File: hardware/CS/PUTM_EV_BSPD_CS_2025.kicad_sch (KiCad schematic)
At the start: 30 parts, among them J1 Conn_01x04, J2 LEM, J3 Conn_01x04, U1 MC78M12CDTG, U2 LM1117IMP-5.0, U3 TLV9354QPWRQ1

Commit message: initial layout for Current Sensor
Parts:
- removed J1: Conn_01x04, symbol Connector_Generic:Conn_01x04
- 24V/500mA1: renamed from 24V/500mA; footprint (none) -> Fuse:Fuse_1812_4532Metric
- C1: footprint (none) -> Capacitor_SMD:C_0805_2012Metric
- C7: footprint (none) -> Capacitor_SMD:C_0603_1608Metric
- D1: footprint Diode_THT:D_DO-201AE_P15.24mm_Horizontal -> Diode_SMD:D_SOD-523
- D2, D3: footprint (none) -> Diode_SMD:D_0603_1608Metric
- J2: footprint (none) -> Snapeda:current_sensor
- J3: footprint (none) -> Snapeda:HARWIN_M80-5100422
- R1, R10, R11, R12, R13, R2, R3, R4, R5, R6, R7, R8, R9: footprint (none) -> Resistor_SMD:R_0603_1608Metric
- U3: footprint (none) -> Snapeda:DYY0014A_TEX-M
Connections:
- net OUT: now reaches U3.13 (-), U3.14
- net OUT: now also J3.3 (Pin_3)
- no-connect marks 4 -> 1
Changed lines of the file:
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@@
 	)
 	(no_connect
-		(at 26.67 27.94)
-	)
-	(no_connect
-		(at 228.6 111.76)
-	)
-	(no_connect
-		(at 228.6 114.3)
-	)
-	(no_connect
 		(at 26.67 30.48)
 	)
@@
 	(wire
 		(pts
+			(xy 26.67 27.94) (xy 29.21 27.94)
+		)
+		(stroke
+			(width 0)
+			(type default)
+		)
+	)
+	(wire
+		(pts
 			(xy 132.08 113.03) (xy 132.08 115.57)
 		)
@@
 		)
 	)
-	(symbol
-		(lib_id "Connector_Generic:Conn_01x04")
-		(at 233.68 111.76 0)
-		(unit 1)
-		(exclude_from_sim no)
-		(in_bom yes)
-		(on_board yes)
-		(dnp no)
-		(fields_autoplaced yes)
-		(property "Reference" "J1"
-			(at 236.22 111.7599 0)
-			(effects
-				(font
-					(size 1.27 1.27)
-				)
-				(justify left)
-			)
-		)
-		(property "Value" "Conn_01x04"
-			(at 236.22 114.2999 0)
-			(effects
-				(font
-					(size 1.27 1.27)
-				)
-				(justify left)
-			)
-		)
-		(property "Footprint" ""
-			(at 233.68 111.76 0)
-			(effects
-				(font
-					(size 1.27 1.27)
-				)
-				(hide yes)
-			)
-		)
-		(property "Datasheet" "~https://www.harwin.com/products/M80-4810405"
-			(at 233.68 111.76 0)
-			(effects
-				(font
-					(size 1.27 1.27)
-				)
-				(hide yes)
-			)
-		)
-		(property "Description" "Generic connector, single row, 01x04, script generated (kicad-library-utils/schlib/autogen/connector/)"
-			(at 233.68 111.76 0)
-			(effects
-				(font
-					(size 1.27 1.27)
-				)
-				(hide yes)
+	(label "OUT"
+		(at 228.6 109.22 0)
+		(effects
+			(font
+				(size 1.27 1.27)
 			)
+			(justify left bottom)
 		)
-		(pin "1"
-		)
-		(pin "3"
-		)
-		(pin "4"
-		)
-		(pin "2"
-		)
-		(instances
-			(project ""
-				(path "/b652b05a-4e3d-4ad1-b032-18886abe7d45"
-					(reference "J1")
-					(unit 1)
-				)
+	)
+	(label "OUT"
+		(at 29.21 27.94 0)
+		(effects
+			(font
+				(size 1.27 1.27)
 			)
+			(justify left bottom)
 		)
 	)
@@
 		(on_board yes)
 		(dnp no)
-		(property "Reference" "24V/500mA"
+		(property "Reference" "24V/500mA1"
 			(at 43.18 27.432 90)
 			(effects
@@
 			)
 		)
-		(property "Footprint" ""
+		(property "Footprint" "Fuse:Fuse_1812_4532Metric"
 			(at 43.18 27.178 90)
 			(effects
@@
 			(project "PUTM_EV_BSPD_CS_2025"
 				(path "/b652b05a-4e3d-4ad1-b032-18886abe7d45"
-					(reference "24V/500mA")
+					(reference "24V/500mA1")
 					(unit 1)
 				)
@@
 			)
 		)
-		(property "Footprint" ""
+		(property "Footprint" "Resistor_SMD:R_0603_1608Metric"
 			(at 178.308 92.71 90)
 			(effects
@@
 	)
 	(symbol
-		(lib_id "power:GND")
-		(at 228.6 116.84 270)
-		(unit 1)
-		(exclude_from_sim no)
-		(in_bom yes)
-		(on_board yes)
-		(dnp no)
-		(fields_autoplaced yes)
-		(property "Reference" "#PWR014"
-			(at 222.25 116.84 0)
-			(effects
-				(font
-					(size 1.27 1.27)
-				)
-				(hide yes)
-			)
-		)
-		(property "Value" "GND"
-			(at 224.79 116.8399 90)
-			(effects
-				(font
-					(size 1.27 1.27)
-				)
-				(justify right)
-			)
-		)
-		(property "Footprint" ""
-			(at 228.6 116.84 0)
-			(effects
-				(font
-					(size 1.27 1.27)
-				)
-				(hide yes)
-			)
-		)
-		(property "Datasheet" ""
-			(at 228.6 116.84 0)
-			(effects
-				(font
-					(size 1.27 1.27)
-				)
-				(hide yes)
-			)
-		)
-		(property "Description" "Power symbol creates a global label with name \"GND\" , ground"
-			(at 228.6 116.84 0)
-			(effects
-				(font
-					(size 1.27 1.27)
-				)
-				(hide yes)
-			)
-		)
-		(pin "1"
-		)
-		(instances
-			(project "PUTM_EV_BSPD_CS_2025"
-				(path "/b652b05a-4e3d-4ad1-b032-18886abe7d45"
-					(reference "#PWR014")
-					(unit 1)
-				)
-			)
-		)
-	)
-	(symbol
 		(lib_id "power:+5V")
 		(at 127 19.05 0)
@@
 			)
 		)
-		(property "Footprint" ""
+		(property "Footprint" "Snapeda:DYY0014A_TEX-M"
 			(at 105.41 106.68 0)
 			(effects
@@
 			)
 		)
-		(property "Footprint" ""
+		(property "Footprint" "Resistor_SMD:R_0603_1608Metric"
 			(at 252.222 24.13 90)
 			(effects
@@
 			)
 		)
-		(property "Footprint" ""
+		(property "Footprint" "Snapeda:DYY0014A_TEX-M"
 			(at 177.8 30.48 0)
 			(effects
@@
 			)
 		)
-		(property "Footprint" ""
+		(property "Footprint" "Resistor_SMD:R_0603_1608Metric"
 			(at 130.302 90.17 90)
 			(effects
@@
 			)
 		)
-		(property "Footprint" ""
+		(property "Footprint" "Resistor_SMD:R_0603_1608Metric"
 			(at 130.302 80.01 90)
 			(effects
@@
 			)
 		)
-		(property "Footprint" ""
+		(property "Footprint" "Resistor_SMD:R_0603_1608Metric"
 			(at 97.028 119.38 90)
 			(effects
@@
 			)
 		)
-		(property "Footprint" ""
+		(property "Footprint" "Diode_SMD:D_0603_1608Metric"
 			(at 176.53 111.76 0)
 			(effects
@@
 			)
 		)
-		(property "Footprint" ""
+		(property "Footprint" "Snapeda:DYY0014A_TEX-M"
 			(at 163.83 87.63 0)
 			(effects
@@
 			)
 		)
-		(property "Footprint" ""
+		(property "Footprint" "Snapeda:current_sensor"
 			(at 229.87 27.94 0)
 			(effects
@@
 			)
 		)
-		(property "Footprint" ""
+		(property "Footprint" "Resistor_SMD:R_0603_1608Metric"
 			(at 252.222 34.29 90)
 			(effects
@@
 			)
 		)
-		(property "Footprint" ""
+		(property "Footprint" "Resistor_SMD:R_0603_1608Metric"
 			(at 86.36 105.918 90)
 			(effects
@@
 			)
 		)
-		(property "Footprint" ""
+		(property "Footprint" "Diode_SMD:D_0603_1608Metric"
 			(at 176.53 100.33 0)
 			(effects
@@
 			)
 		)
-		(property "Footprint" ""
+		(property "Footprint" "Resistor_SMD:R_0603_1608Metric"
 			(at 139.7 108.458 90)
 			(effects
@@
 			)
 		)
-		(property "Footprint" ""
+		(property "Footprint" "Resistor_SMD:R_0603_1608Metric"
 			(at 86.36 110.998 90)
 			(effects
@@
 			)
 		)
-		(property "Footprint" ""
+		(property "Footprint" "Resistor_SMD:R_0603_1608Metric"
 			(at 178.308 119.38 90)
 			(effects
@@
 			)
 		)
-		(property "Footprint" ""
+		(property "Footprint" "Resistor_SMD:R_0603_1608Metric"
 			(at 130.302 129.54 90)
 			(effects
@@
 			)
 		)
-		(property "Footprint" ""
+		(property "Footprint" "Resistor_SMD:R_0603_1608Metric"
 			(at 106.68 94.488 90)
 			(effects
@@
 			)
 		)
-		(property "Footprint" ""
+		(property "Footprint" "Capacitor_SMD:C_0805_2012Metric"
 			(at 61.9252 34.29 0)
 			(effects
@@
 			)
 		)
-		(property "Footprint" ""
+		(property "Footprint" "Resistor_SMD:R_0603_1608Metric"
 			(at 130.302 119.38 90)
 			(effects
@@
 			)
 		)
-		(property "Footprint" "Diode_THT:D_DO-201AE_P15.24mm_Horizontal"
+		(property "Footprint" "Diode_SMD:D_SOD-523"
 			(at 46.99 30.48 0)
 			(effects
@@
 			)
 		)
-		(property "Footprint" ""
+		(property "Footprint" "Snapeda:HARWIN_M80-5100422"
 			(at 21.59 30.48 0)
 			(effects
@@
 			)
 		)
-		(property "Footprint" ""
+		(property "Footprint" "Snapeda:DYY0014A_TEX-M"
 			(at 162.56 123.19 0)
 			(effects
@@
 			)
 		)
-		(property "Footprint" ""
+		(property "Footprint" "Capacitor_SMD:C_0603_1608Metric"
 			(at 162.2552 34.29 0)
 			(effects
@@
 			)
 		)
-		(property "Footprint" ""
+		(property "Footprint" "Snapeda:DYY0014A_TEX-M"
 			(at 204.47 109.22 0)
 			(effects

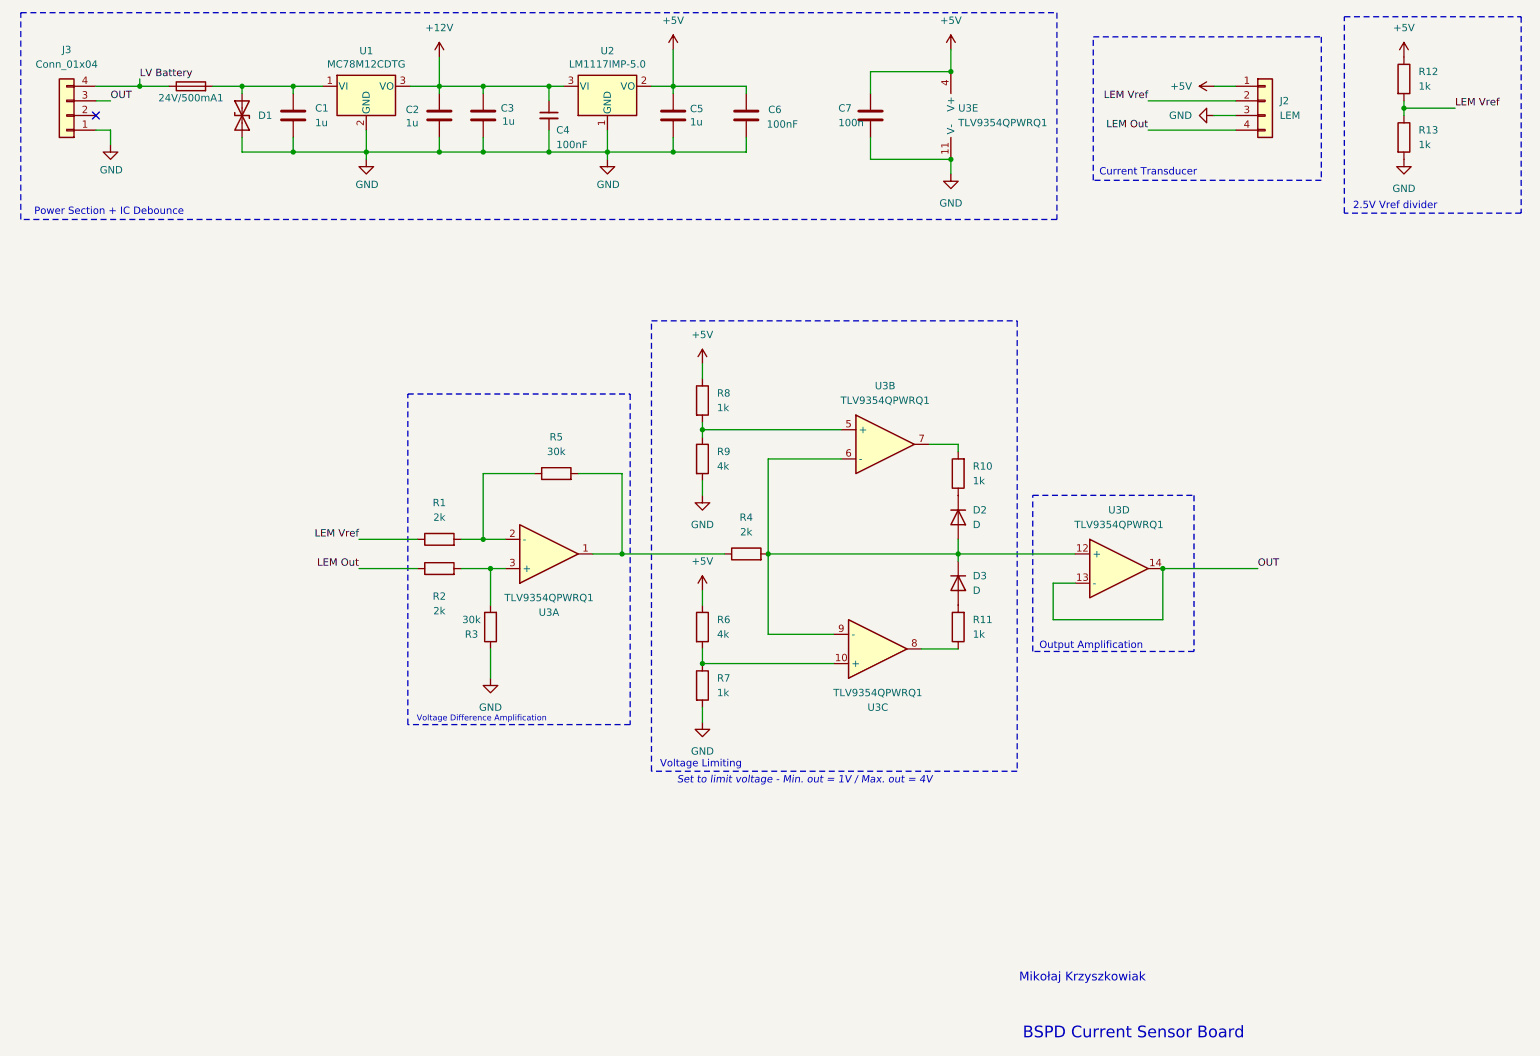
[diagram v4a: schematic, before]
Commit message: Small changes in scheme and added vias
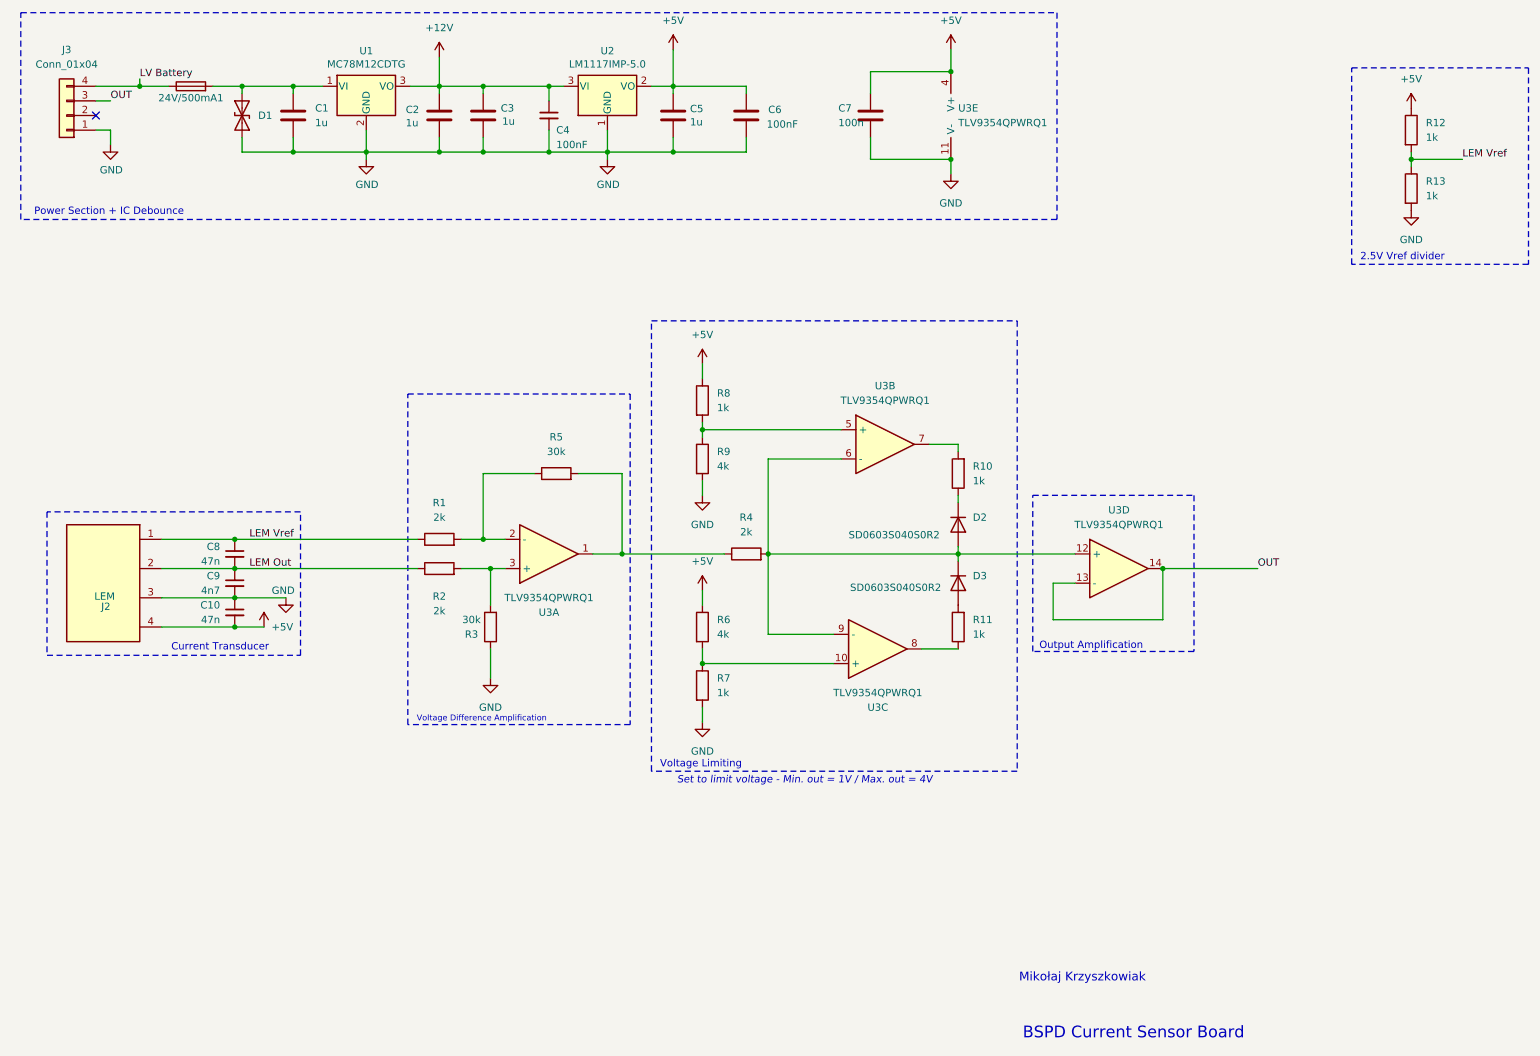
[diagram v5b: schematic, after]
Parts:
- added C10, C8: 47n, Capacitor_SMD:C_0603_1608Metric_Pad1.08x0.95mm_HandSolder, symbol Device:C_Small
- added C9: 4n7, Capacitor_SMD:C_0603_1608Metric_Pad1.08x0.95mm_HandSolder, symbol Device:C_Small
- D2, D3: value D -> SD0603S040S0R2
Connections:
- net +5V: now also J2.4 (Pin_4), C10.2; no longer J2.1 (Pin_1)
- net GND: now also C10.1, C9.2
- net LEM Out: now also J2.2 (Pin_2), C8.2, C9.1; no longer J2.4 (Pin_4)
- net LEM Vref: now also J2.1 (Pin_1), C8.1; no longer J2.2 (Pin_2)
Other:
- moved on the sheet: D2, R12, R13

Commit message: Added TVS Protection to output, change layout of omp amp
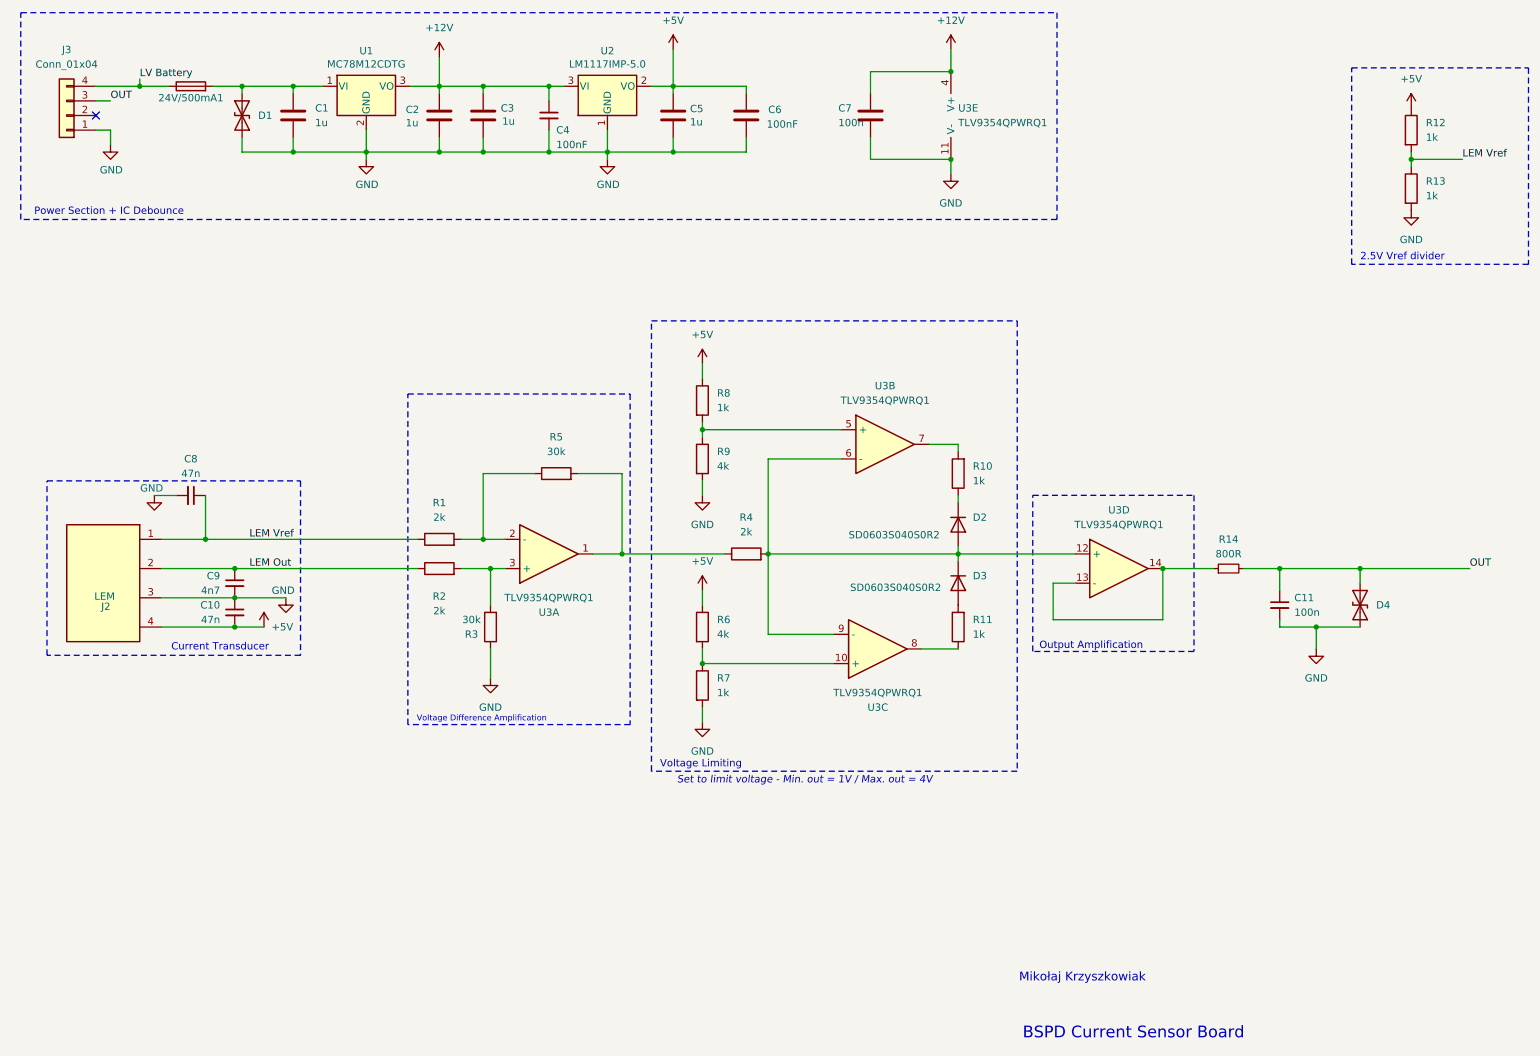
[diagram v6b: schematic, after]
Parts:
- added C11: 100n, Capacitor_SMD:C_0603_1608Metric_Pad1.08x0.95mm_HandSolder, symbol Device:C_Small
- added D4: TESDU5V0 RGG, Diode_SMD:D_0603_1608Metric, symbol Diode:1N630xCA
- added R14: 800R, Resistor_SMD:R_0603_1608Metric_Pad0.98x0.95mm_HandSolder, symbol Device:R_Small
- U3: footprint Snapeda:DYY0014A_TEX-M -> Snapeda:SOP65P640X120-14N
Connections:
- net +12V: now also C7.1, U3.4 (V+)
- net +5V: no longer C7.1, U3.4 (V+)
- net GND: now also C8.2, C11.2, D4.2 (A2)
- net LEM Out: no longer C8.2
- net OUT: now also C11.1, D4.1 (A1), R14.2; no longer U3.13 (-), U3.14
- new net: R14.1, U3.13 (-), U3.14
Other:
- moved on the sheet: C8
